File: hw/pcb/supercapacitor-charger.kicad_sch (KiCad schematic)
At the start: 11 parts, among them U2 TPS61094

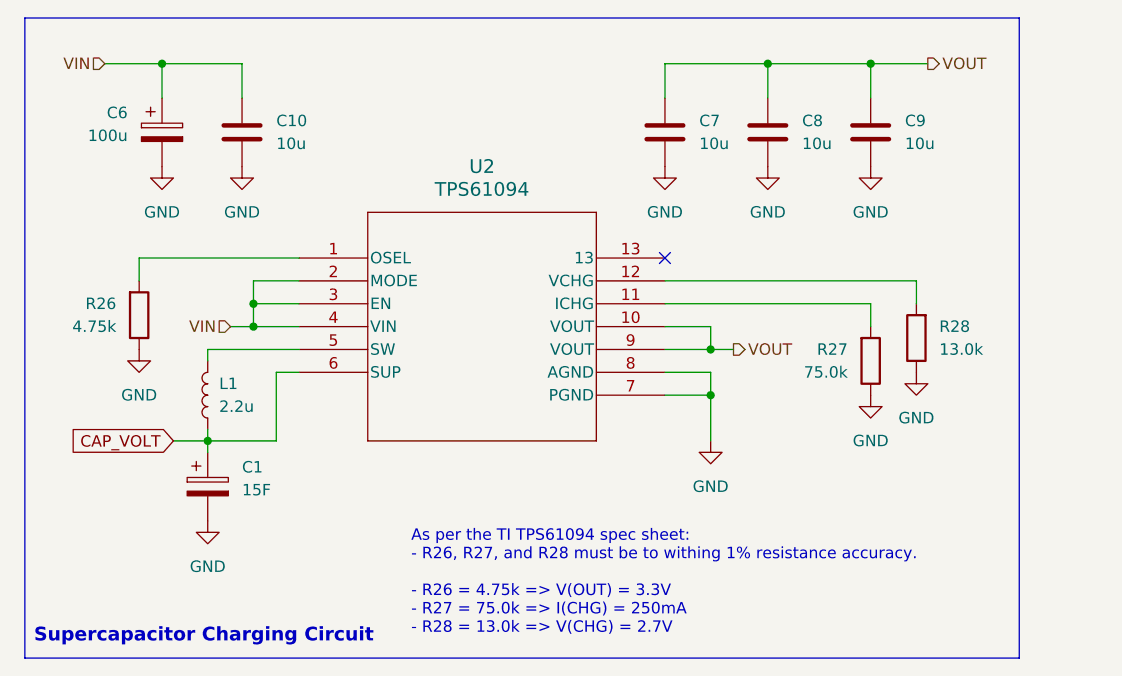
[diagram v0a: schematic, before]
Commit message: fix: rewired swd pins and supercap changer enable pins
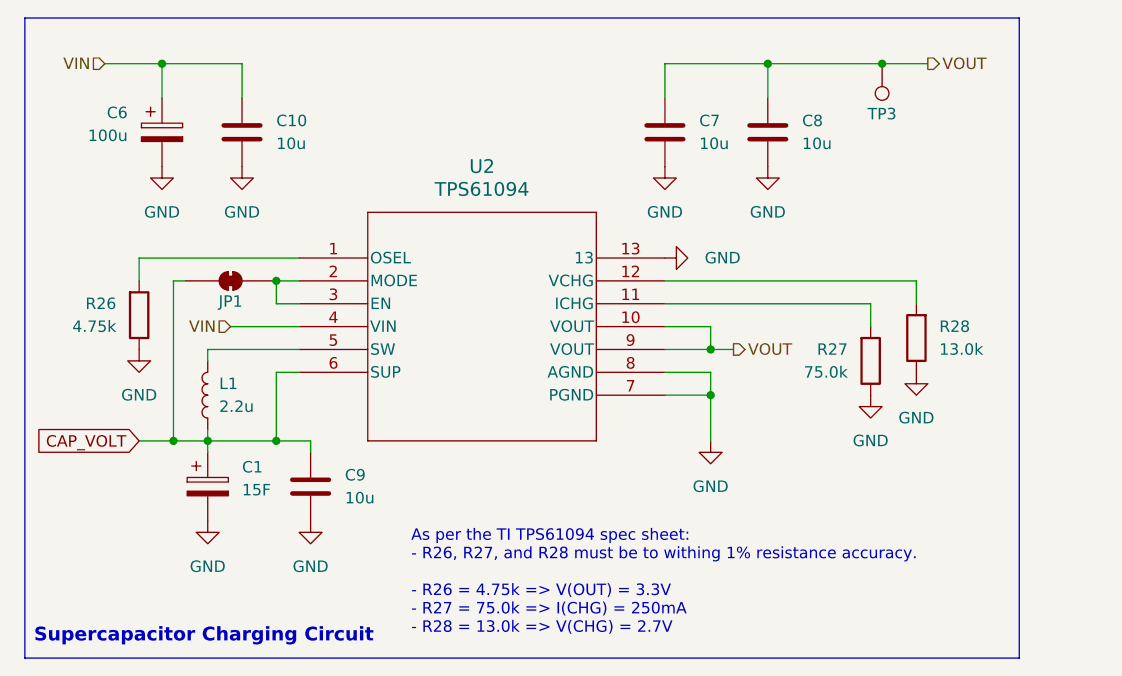
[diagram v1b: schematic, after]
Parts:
- added JP1: SolderJumper_2_Bridged, Jumper:SolderJumper-2_P1.3mm_Bridged_RoundedPad1.0x1.5mm, symbol Jumper:SolderJumper_2_Bridged
- added TP3: TestPoint, TestPoint:TestPoint_Pad_D1.0mm, symbol Connector:TestPoint
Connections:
- net CAP_VOLT: now also C9.1, JP1.1 (A)
- net GND: now also U2.13
- net VIN: no longer U2.2 (MODE), U2.3 (EN)
- net VOUT: now also TP3.1; no longer C9.1
- new net: JP1.2 (B), U2.2 (MODE), U2.3 (EN)
- no-connect marks 1 -> 0
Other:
- company: (none) -> Isaac Pawley
